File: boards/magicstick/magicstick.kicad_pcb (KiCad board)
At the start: 2 copper layers, 22 parts, among them Q1 2N2222, Q2 2N2222, Q3 2N2222, Q4 2N2907, Q5 2N2907, Q6 2N2907, U1 NodeMCU_Amica_R2

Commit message: pcb for magic stick
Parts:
- moved RFID1 17.8 mm to (108.0, 85.1), turned to 180 degrees
- moved D2 15.3 mm to (175.3, 86.4), turned to 180 degrees
- moved R5 14.2 mm to (157.5, 66.0)
- moved R8 14.2 mm to (157.5, 80.0)
- moved D1 14.2 mm to (175.3, 68.6)
- moved R10 14.2 mm to (157.5, 83.8)
- moved R6 14.2 mm to (157.5, 73.7)
- moved R7 14.2 mm to (157.5, 69.8)
- moved R9 14.2 mm to (157.5, 87.6)
- moved R1 10.2 mm to (124.5, 69.8), turned to 180 degrees
- moved R2 10.2 mm to (124.5, 77.5), turned to 180 degrees
- moved R3 10.2 mm to (124.5, 83.8), turned to 180 degrees
- moved Q5 2.59 mm to (149.9, 77.5)
- moved Q4 2.54 mm to (149.9, 69.8)
- moved Q6 2.54 mm to (149.9, 83.8)
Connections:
- net Net-(U1-Pad25) renamed +3V3
- D2 pad 2: Net-(D2-Pad2) -> GND
- U1 pad 14: Net-(U1-Pad14) -> GND
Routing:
- net GND: track 0.00 -> 126.4 mm
- net Net-(RFID1-Pad8): track 0.00 -> 47.1 mm
- net Net-(RFID1-Pad2): track 0.00 -> 40.0 mm
- net Net-(RFID1-Pad3): track 0.00 -> 39.6 mm
- net Net-(RFID1-Pad4): track 0.00 -> 39.0 mm
- net Net-(R3-Pad2): track 0.00 -> 37.4 mm
- net Net-(RFID1-Pad1): track 0.00 -> 31.9 mm
- net +5V: track 0.00 -> 20.3 mm
- net Net-(Q6-Pad3): track 0.00 -> 20.2 mm
- net Net-(Q4-Pad3): track 0.00 -> 19.8 mm
- net Net-(Q5-Pad3): track 0.00 -> 19.7 mm
- net Net-(R2-Pad2): track 0.00 -> 18.1 mm
- net Net-(RFID1-Pad7): track 0.00 -> 15.8 mm
- net Net-(D2-Pad1): track 0.00 -> 15.3 mm
- net Net-(R1-Pad2): track 0.00 -> 11.3 mm
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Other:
- board outline added: 77.5 x 30.5 mm

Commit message: magic stick updates
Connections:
- U1 pad 10: Net-(U1-Pad10) -> GND
- U1 pad 24: Net-(U1-Pad24) -> GND
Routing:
- net GND: track 126.4 -> 131.7 mm
- net Net-(RFID1-Pad2): track 40.0 -> 43.0 mm
- net Net-(Q4-Pad3): track 19.8 -> 21.5 mm
- net Net-(Q5-Pad3): track 19.7 -> 18.6 mm
- net Net-(RFID1-Pad3): track 39.6 -> 40.5 mm
- net Net-(R2-Pad2): track 18.1 -> 17.5 mm
- net Net-(RFID1-Pad4): track 39.0 -> 38.3 mm
- net Net-(Q6-Pad3): track 20.2 -> 19.6 mm

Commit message: initial mother board
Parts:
- added R13: 10k, Resistors_ThroughHole:Resistor_Horizontal_RM10mm, F.Cu at (177.7, 50.2)
- added R14: 10k, Resistors_ThroughHole:Resistor_Horizontal_RM10mm, F.Cu at (177.7, 47.3)
- added R15: 10k, Resistors_ThroughHole:Resistor_Horizontal_RM10mm, F.Cu at (177.7, 44.4)
- D1, RFID1: moved to B.Cu
- moved U1 88.5 mm to (192.5, 39.8), turned to 270 degrees
- moved RFID1 58.0 mm to (147.8, 42.9)
- moved D2 49.1 mm to (201.3, 44.7), turned to 0 degrees
- moved R9 47.5 mm to (186.2, 49.8)
- moved R8 46.3 mm to (186.2, 43.7)
- moved Q3 45.8 mm to (161.9, 51.4)
- moved R12 44.1 mm to (177.7, 53.1)
- moved R3 43.3 mm to (158.1, 56.5), turned to 90 degrees
- moved Q6 41.4 mm to (180.6, 56.1)
- moved Q5 40.1 mm to (180.6, 51.7)
- moved R10 40.1 mm to (186.2, 55.9)
- moved Q1 39.6 mm to (161.9, 47.0)
- moved Q2 38.6 mm to (161.9, 55.9)
- moved R11 38.2 mm to (177.7, 56.1)
- moved Q4 38.2 mm to (180.6, 47.2)
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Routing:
- net GND: track 131.7 -> 0.00 mm
- net Net-(RFID1-Pad8): track 47.1 -> 0.00 mm
- net Net-(RFID1-Pad2): track 43.0 -> 0.00 mm
- net Net-(RFID1-Pad3): track 40.5 -> 0.00 mm
- net Net-(RFID1-Pad4): track 38.3 -> 0.00 mm
- net Net-(R3-Pad2): track 37.8 -> 0.00 mm
- net Net-(RFID1-Pad1): track 31.9 -> 0.00 mm
- net Net-(Q4-Pad3): track 21.5 -> 0.00 mm
- net +5V: track 20.3 -> 0.00 mm
- net Net-(Q6-Pad3): track 19.6 -> 0.00 mm
- net Net-(Q5-Pad3): track 18.6 -> 0.00 mm
- net Net-(R2-Pad2): track 17.5 -> 0.00 mm
- net Net-(RFID1-Pad7): track 15.8 -> 0.00 mm
- net Net-(D2-Pad1): track 15.3 -> 0.00 mm
- net Net-(R1-Pad2): track 11.3 -> 0.00 mm
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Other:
- board size 77.5 x 30.5 mm -> 58.4 x 26.7 mm
- net class Power added: clearance 0.2, trace_width 0.5, via_dia 0.6, via_drill 0.4

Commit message: another revision
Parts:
- added REF1: MountingHole_2-5mm, Mounting_Holes:MountingHole_2-5mm, F.Cu at (152.7, 40.9)
- added REF3: MountingHole_2-5mm, Mounting_Holes:MountingHole_2-5mm, F.Cu at (200.9, 62.0)
- added REF4: MountingHole_2-5mm, Mounting_Holes:MountingHole_2-5mm, F.Cu at (200.9, 40.9)
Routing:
- net GND: track 0.00 -> 107.7 mm
- net Net-(RFID1-Pad1): track 0.00 -> 58.4 mm
- net Net-(R1-Pad2): track 0.00 -> 50.3 mm, vias 0 -> 1
- net Net-(RFID1-Pad2): track 0.00 -> 47.6 mm
- net Net-(RFID1-Pad7): track 0.00 -> 45.0 mm
- net Net-(R2-Pad2): track 0.00 -> 41.6 mm
- net Net-(RFID1-Pad4): track 0.00 -> 41.1 mm
- net +5V: track 0.00 -> 40.9 mm
- net Net-(RFID1-Pad3): track 0.00 -> 37.8 mm
- net Net-(R3-Pad2): track 0.00 -> 26.5 mm
- net Net-(Q4-Pad2): track 0.00 -> 22.5 mm
- net Net-(Q5-Pad2): track 0.00 -> 16.8 mm
- net Net-(D1-Pad1): track 0.00 -> 16.0 mm
- net Net-(Q1-Pad2): track 0.00 -> 16.0 mm
- net Net-(Q6-Pad2): track 0.00 -> 15.2 mm
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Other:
- board text added: "1K Ω"
- board text added: "2xR;2xG;2xB"
- board text added: "3x10k;3x1k"
- board text added: "npn"
- board text added: "pnp"

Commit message: pcb v1
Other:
- board text added: "3.3v"
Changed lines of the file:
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@@
     (links 48)
     (no_connects 0)
-    (area 142.838715 33.481 205.562096 64.845001)
+    (area 142.838715 33.481 209.597584 66.55018)
     (thickness 1.6)
-    (drawings 9)
+    (drawings 10)
     (tracks 199)
     (zones 0)
@@
     (visible_elements FFFFFF7F)
     (pcbplotparams
-      (layerselection 0x00030_80000001)
+      (layerselection 0x010f0_80000001)
       (usegerberextensions false)
       (excludeedgelayer true)
@@
       (outputformat 1)
       (mirror false)
-      (drillshape 1)
+      (drillshape 0)
       (scaleselection 1)
-      (outputdirectory ""))
+      (outputdirectory gerber))
   )
   (net 0 "")
@@
       (effects (font (size 1 1) (thickness 0.15)))
     )
-    (fp_text value MountingHole_2-5mm (at 0.09906 3.59918) (layer F.Fab)
+    (fp_text value MountingHole_2-5mm (at 0.09906 3.59918) (layer F.Fab) hide
       (effects (font (size 1 1) (thickness 0.15)))
     )
@@
       (effects (font (size 1 1) (thickness 0.15)))
     )
-    (fp_text value MountingHole_2-5mm (at 0.09906 3.59918) (layer F.Fab)
+    (fp_text value MountingHole_2-5mm (at 0.09906 3.59918) (layer F.Fab) hide
       (effects (font (size 1 1) (thickness 0.15)))
     )
@@
     (descr "5mm common cathode RGB LED")
     (tags "RGB LED 5mm Common Cathode")
-    (fp_text reference D1 (at 0 2.25) (layer B.SilkS)
+    (fp_text reference D1 (at 0 2.25) (layer B.SilkS) hide
       (effects (font (size 1 1) (thickness 0.15)) (justify mirror))
     )
-    (fp_text value LED_RCBG (at 0 -6.25) (layer B.Fab)
+    (fp_text value LED_RCBG (at 0 -6.25) (layer B.Fab) hide
       (effects (font (size 1 1) (thickness 0.15)) (justify mirror))
     )
@@
     (descr "5mm common cathode RGB LED")
     (tags "RGB LED 5mm Common Cathode")
-    (fp_text reference D2 (at 0 -2.25) (layer F.SilkS)
-      (effects (font (size 1 1) (thickness 0.15)))
-    )
-    (fp_text value LED_RCBG (at 0 6.25) (layer F.Fab)
+    (fp_text reference D2 (at 0 -2.25) (layer F.SilkS) hide
+      (effects (font (size 1 1) (thickness 0.15)))
+    )
+    (fp_text value LED_RCBG (at 0 6.25) (layer F.Fab) hide
       (effects (font (size 1 1) (thickness 0.15)))
     )
@@
     (descr "Through hole pin header")
     (tags "pin header")
-    (fp_text reference RFID1 (at 0 5.1 180) (layer B.SilkS)
+    (fp_text reference RFID1 (at 0 5.1 180) (layer B.SilkS) hide
       (effects (font (size 1 1) (thickness 0.15)) (justify mirror))
     )
@@
       (effects (font (size 1 1) (thickness 0.15)))
     )
-    (fp_text value MountingHole_2-5mm (at 0.09906 3.59918) (layer F.Fab)
+    (fp_text value MountingHole_2-5mm (at 0.09906 3.59918) (layer F.Fab) hide
       (effects (font (size 1 1) (thickness 0.15)))
     )
     (fp_circle (center 0 0) (end 2.5 0) (layer Cmts.User) (width 0.381))
     (pad 1 thru_hole circle (at 0 0) (size 2.5 2.5) (drill 2.5) (layers))
+  )
+  (gr_text 3.3v (at 147.701 63.5) (layer B.SilkS)
+    (effects (font (size 1 1) (thickness 0.2)) (justify mirror))
   )
   (gr_text 2xR;2xG;2xB (at 191.643 41.91) (layer F.SilkS)
@@
   (segment (start 196.5683 54.1967) (end 200.2712 57.8996) (width 0.25) (layer F.Cu) (net 1))
   (segment (start 195.7724 54.1967) (end 196.5683 54.1967) (width 0.25) (layer F.Cu) (net 1))
-  (segment (start 195.0171 53.4414) (end 195.7724 54.1967) (width 0.25) (layer F.Cu) (net 1))
-  (segment (start 195.0171 48.0609) (end 195.0171 53.4414) (width 0.25) (layer F.Cu) (net 1))
-  (segment (start 196.342 46.736) (end 195.0171 48.0609) (width 0.25) (layer F.Cu) (net 1))
+  (segment (start 194.691 53.086) (end 195.7724 54.1967) (width 0.25) (layer F.Cu) (net 1))
+  (segment (start 194.564 48.514) (end 194.691 53.086) (width 0.25) (layer F.Cu) (net 1))
+  (segment (start 196.342 46.736) (end 194.564 48.514) (width 0.25) (layer F.Cu) (net 1))
   (segment (start 201.549 58.293) (end 200.2712 58.293) (width 0.25) (layer F.Cu) (net 1))
   (segment (start 202.9518 46.228) (end 202.9518 57.023) (width 0.5) (layer B.Cu) (net 2))

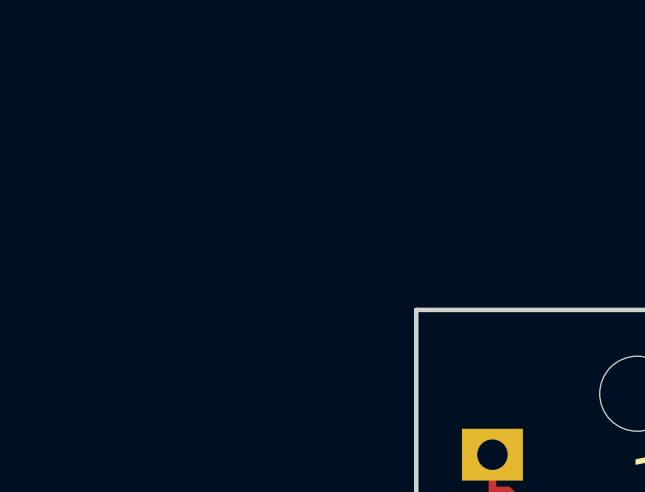
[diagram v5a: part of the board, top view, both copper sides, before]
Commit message: fixed cc foot print; now need to redo motherboard :(
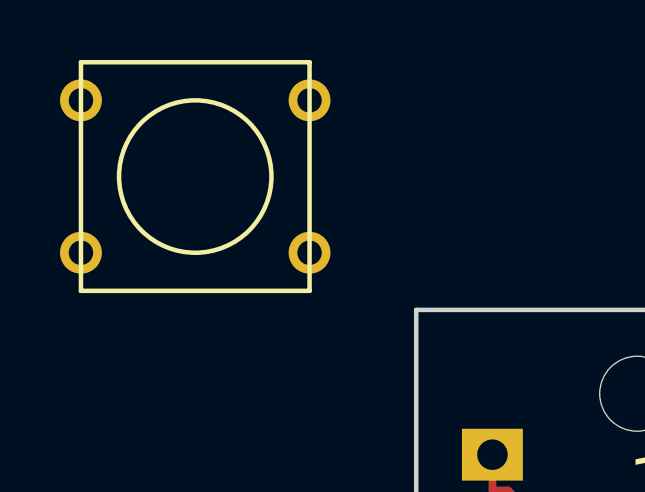
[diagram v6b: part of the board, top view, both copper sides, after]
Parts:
- added SW1: SW_PUSH, Buttons_Switches_ThroughHole:SW_PUSH_SMALL, F.Cu at (137.9, 33.7)
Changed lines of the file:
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@@
 (kicad_pcb (version 4) (host pcbnew 4.0.2-stable)
   (general
-    (links 48)
-    (no_connects 0)
-    (area 142.838715 33.481 209.597584 66.55018)
+    (links 52)
+    (no_connects 4)
+    (area 145.212999 38.024999 203.783001 64.845001)
     (thickness 1.6)
     (drawings 10)
     (tracks 199)
     (zones 0)
-    (modules 28)
+    (modules 29)
     (nets 47)
   )
@@
   (net 32 "Net-(U1-Pad2)")
   (net 33 "Net-(U1-Pad3)")
-  (net 34 "Net-(U1-Pad4)")
-  (net 35 "Net-(U1-Pad5)")
-  (net 36 "Net-(U1-Pad6)")
-  (net 37 "Net-(U1-Pad7)")
-  (net 38 "Net-(U1-Pad8)")
-  (net 39 "Net-(U1-Pad9)")
-  (net 40 "Net-(U1-Pad11)")
-  (net 41 "Net-(U1-Pad12)")
-  (net 42 "Net-(U1-Pad13)")
-  (net 43 "Net-(U1-Pad18)")
-  (net 44 "Net-(U1-Pad19)")
-  (net 45 "Net-(U1-Pad26)")
-  (net 46 +3V3)
+  (net 34 "Net-(U1-Pad5)")
+  (net 35 "Net-(U1-Pad6)")
+  (net 36 "Net-(U1-Pad7)")
+  (net 37 "Net-(U1-Pad8)")
+  (net 38 "Net-(U1-Pad9)")
+  (net 39 "Net-(U1-Pad11)")
+  (net 40 "Net-(U1-Pad12)")
+  (net 41 "Net-(U1-Pad13)")
+  (net 42 "Net-(U1-Pad18)")
+  (net 43 "Net-(U1-Pad19)")
+  (net 44 "Net-(U1-Pad26)")
+  (net 45 +3V3)
+  (net 46 "Net-(SW1-Pad2)")
   (net_class Default "This is the default net class."
     (clearance 0.2)
@@
     (add_net "Net-(RFID1-Pad7)")
     (add_net "Net-(RFID1-Pad8)")
+    (add_net "Net-(SW1-Pad2)")
     (add_net "Net-(U1-Pad1)")
     (add_net "Net-(U1-Pad11)")
@@
     (add_net "Net-(U1-Pad26)")
     (add_net "Net-(U1-Pad3)")
-    (add_net "Net-(U1-Pad4)")
     (add_net "Net-(U1-Pad5)")
     (add_net "Net-(U1-Pad6)")
@@
       (net 33 "Net-(U1-Pad3)"))
     (pad 4 thru_hole oval (at 0 7.62 270) (size 2.032 1.7272) (drill 1.016) (layers *.Cu *.Mask F.SilkS)
-      (net 34 "Net-(U1-Pad4)"))
+      (net 46 "Net-(SW1-Pad2)"))
     (pad 5 thru_hole oval (at 0 10.16 270) (size 2.032 1.7272) (drill 1.016) (layers *.Cu *.Mask F.SilkS)
-      (net 35 "Net-(U1-Pad5)"))
+      (net 34 "Net-(U1-Pad5)"))
     (pad 6 thru_hole oval (at 0 12.7 270) (size 2.032 1.7272) (drill 1.016) (layers *.Cu *.Mask F.SilkS)
-      (net 36 "Net-(U1-Pad6)"))
+      (net 35 "Net-(U1-Pad6)"))
     (pad 7 thru_hole oval (at 0 15.24 270) (size 2.032 1.7272) (drill 1.016) (layers *.Cu *.Mask F.SilkS)
-      (net 37 "Net-(U1-Pad7)"))
+      (net 36 "Net-(U1-Pad7)"))
     (pad 8 thru_hole oval (at 0 17.78 270) (size 2.032 1.7272) (drill 1.016) (layers *.Cu *.Mask F.SilkS)
-      (net 38 "Net-(U1-Pad8)"))
+      (net 37 "Net-(U1-Pad8)"))
     (pad 9 thru_hole oval (at 0 20.32 270) (size 2.032 1.7272) (drill 1.016) (layers *.Cu *.Mask F.SilkS)
-      (net 39 "Net-(U1-Pad9)"))
+      (net 38 "Net-(U1-Pad9)"))
     (pad 10 thru_hole oval (at 0 22.86 270) (size 2.032 1.7272) (drill 1.016) (layers *.Cu *.Mask F.SilkS)
       (net 2 GND))
     (pad 11 thru_hole oval (at 0 25.4 270) (size 2.032 1.7272) (drill 1.016) (layers *.Cu *.Mask F.SilkS)
-      (net 40 "Net-(U1-Pad11)"))
+      (net 39 "Net-(U1-Pad11)"))
     (pad 12 thru_hole oval (at 0 27.94 270) (size 2.032 1.7272) (drill 1.016) (layers *.Cu *.Mask F.SilkS)
-      (net 41 "Net-(U1-Pad12)"))
+      (net 40 "Net-(U1-Pad12)"))
     (pad 13 thru_hole oval (at 0 30.48 270) (size 2.032 1.7272) (drill 1.016) (layers *.Cu *.Mask F.SilkS)
-      (net 42 "Net-(U1-Pad13)"))
+      (net 41 "Net-(U1-Pad13)"))
     (pad 14 thru_hole oval (at 0 33.02 270) (size 2.032 1.7272) (drill 1.016) (layers *.Cu *.Mask F.SilkS)
       (net 2 GND))
@@
       (net 24 "Net-(RFID1-Pad1)"))
     (pad 18 thru_hole oval (at 22.86 30.48 270) (size 2.032 1.7272) (drill 1.016) (layers *.Cu *.Mask F.SilkS)
-      (net 43 "Net-(U1-Pad18)"))
+      (net 42 "Net-(U1-Pad18)"))
     (pad 17 thru_hole oval (at 22.86 33.02 270) (size 2.032 1.7272) (drill 1.016) (layers *.Cu *.Mask F.SilkS)
       (net 2 GND))
     (pad 19 thru_hole oval (at 22.86 27.94 270) (size 2.032 1.7272) (drill 1.016) (layers *.Cu *.Mask F.SilkS)
-      (net 44 "Net-(U1-Pad19)"))
+      (net 43 "Net-(U1-Pad19)"))
     (pad 25 thru_hole oval (at 22.86 12.7 270) (size 2.032 1.7272) (drill 1.016) (layers *.Cu *.Mask F.SilkS)
-      (net 46 +3V3))
+      (net 45 +3V3))
     (pad 26 thru_hole oval (at 22.86 10.16 270) (size 2.032 1.7272) (drill 1.016) (layers *.Cu *.Mask F.SilkS)
-      (net 45 "Net-(U1-Pad26)"))
+      (net 44 "Net-(U1-Pad26)"))
     (pad 24 thru_hole oval (at 22.86 15.24 270) (size 2.032 1.7272) (drill 1.016) (layers *.Cu *.Mask F.SilkS)
       (net 2 GND))
@@
     (pad 1 thru_hole circle (at 0 0) (size 2.5 2.5) (drill 2.5) (layers))
   )
+  (module Buttons_Switches_ThroughHole:SW_PUSH_SMALL (layer F.Cu)
+    (at 137.922 33.655)
+    (fp_text reference SW1 (at 0 -0.762) (layer F.SilkS) hide
+      (effects (font (size 1 1) (thickness 0.15)))
+    )
+    (fp_text value SW_PUSH (at 0 1.016) (layer F.Fab) hide
+      (effects (font (size 1 1) (thickness 0.15)))
+    )
+    (fp_circle (center 0 0) (end 0 -2.54) (layer F.SilkS) (width 0.15))
+    (fp_line (start -3.81 -3.81) (end 3.81 -3.81) (layer F.SilkS) (width 0.15))
+    (fp_line (start 3.81 -3.81) (end 3.81 3.81) (layer F.SilkS) (width 0.15))
+    (fp_line (start 3.81 3.81) (end -3.81 3.81) (layer F.SilkS) (width 0.15))
+    (fp_line (start -3.81 -3.81) (end -3.81 3.81) (layer F.SilkS) (width 0.15))
+    (pad 1 thru_hole circle (at 3.81 -2.54) (size 1.397 1.397) (drill 0.8128) (layers *.Cu *.Mask F.SilkS)
+      (net 2 GND))
+    (pad 2 thru_hole circle (at 3.81 2.54) (size 1.397 1.397) (drill 0.8128) (layers *.Cu *.Mask F.SilkS)
+      (net 46 "Net-(SW1-Pad2)"))
+    (pad 1 thru_hole circle (at -3.81 -2.54) (size 1.397 1.397) (drill 0.8128) (layers *.Cu *.Mask F.SilkS)
+      (net 2 GND))
+    (pad 2 thru_hole circle (at -3.81 2.54) (size 1.397 1.397) (drill 0.8128) (layers *.Cu *.Mask F.SilkS)
+      (net 46 "Net-(SW1-Pad2)"))
+  )
   (gr_text 3.3v (at 147.701 63.5) (layer B.SilkS)
